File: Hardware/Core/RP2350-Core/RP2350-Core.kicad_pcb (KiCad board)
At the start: 2 copper layers, 62 parts, among them CN10 PR5L4015-5P-C-F, CN11 PR5L4015-5P-C-F, CN7 PR5L4015-5P-C-F, CN8 PR5L4015-5P-C-F, CN9 PR5L4015-5P-C-F, J7 SWD, J9 Conn_01x10_Socket, Q2 2N7002, Q3 2N7002, SW1 TS-1187A-B-A-B, SW2 TS-1187A-B-A-B, U19 W25Q16JVSNIQ, U2 AP2112K-3.3, U3 LM66200DRLR, U35 PR5L5015-5P-C-H, U36 PR5L5015-5P-C-H, U37 PR5L5015-5P-C-H, U38 PR5L5015-5P-C-H, U39 PR5L5015-5P-C-H, U4 RP2350A, Y1 Crystal

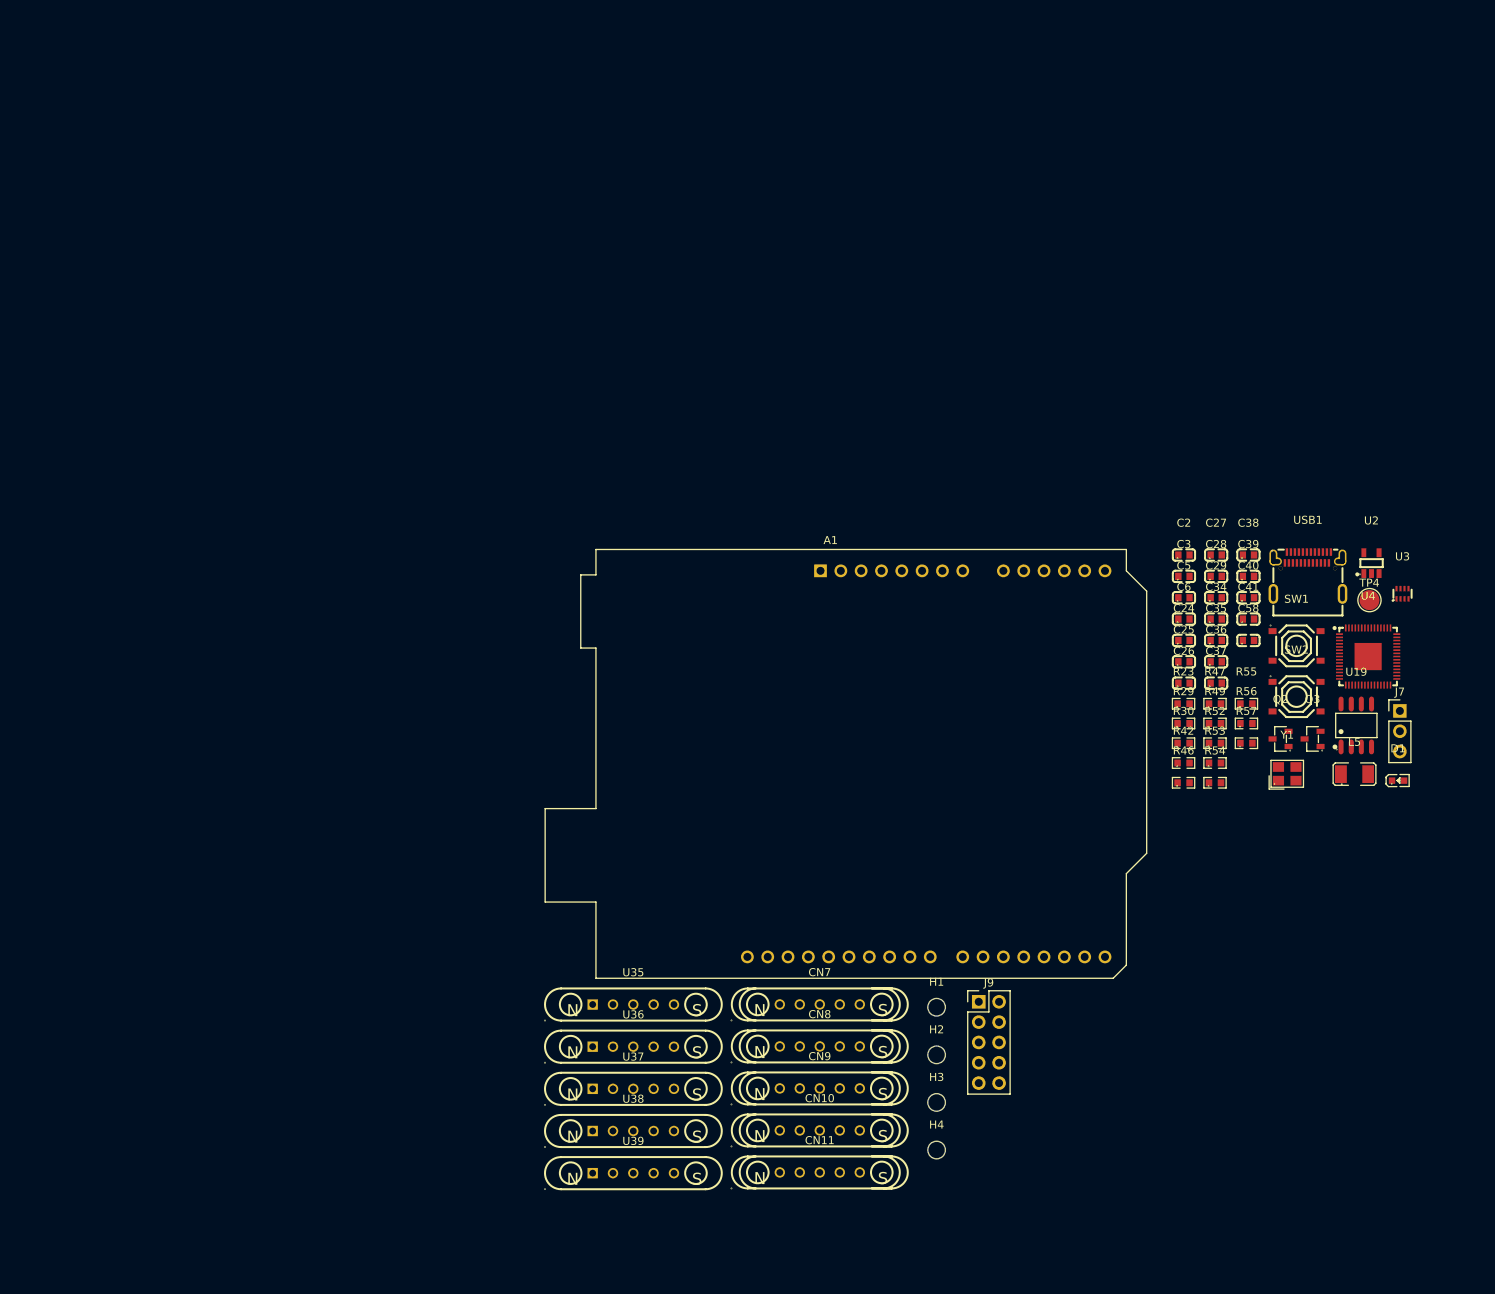
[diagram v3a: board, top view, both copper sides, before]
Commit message: Placed footprints RP235x
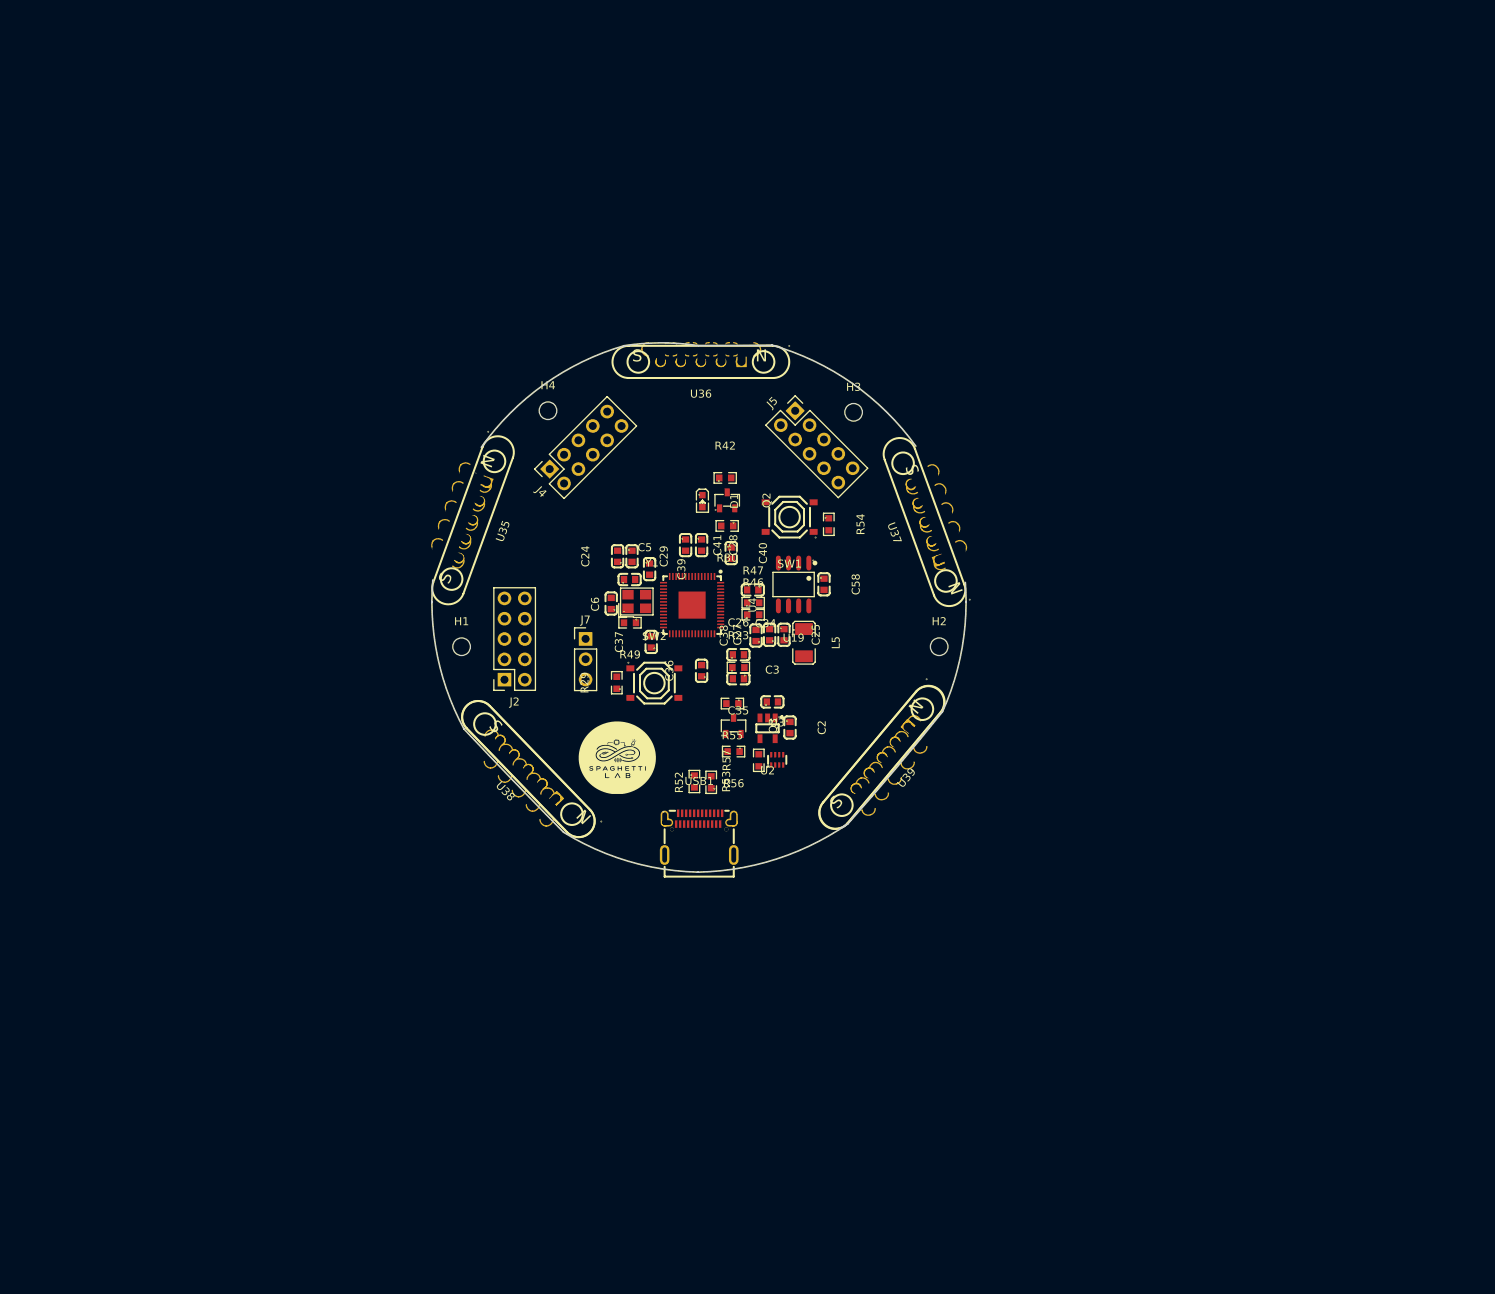
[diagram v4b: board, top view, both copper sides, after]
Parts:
- removed A1: Arduino_UNO_R3, Module:Arduino_UNO_R3
- removed J9: Conn_01x10_Socket, Connector_PinHeader_2.54mm:PinHeader_2x05_P2.54mm_Vertical
- removed TP4: ~, TestPoint:TestPoint_Pad_D2.5mm
- added ?: , Pad_e185, F.Cu at (66.4, 94.8)
- added ?: , Pad_e189, F.Cu at (59.4, 87.6)
- added ?: , Pad_e166, F.Cu at (54.8, 60.7)
- added ?: , Pad_e182, F.Cu at (109.5, 89.6)
- added ?: , Pad_e180, F.Cu at (112.6, 85.8)
- added ?: , Pad_e168, F.Cu at (56.5, 56.0)
- added ?: , Pad_e188, F.Cu at (61.2, 89.4)
- added ?: , Pad_e184, F.Cu at (106.2, 93.5)
- added ?: , Pad_e186, F.Cu at (64.7, 93.0)
- added ?: , Pad_e174, F.Cu at (113.3, 53.9)
- added ?: , Pad_e187, F.Cu at (62.9, 91.2)
- added ?: , Pad_e172, F.Cu at (115.1, 58.7)
- added ?: , Pad_e177, F.Cu at (85.7, 37.6)
- added ?: , Pad_e179, F.Cu at (80.6, 37.6)
- added ?: , Pad_e178, F.Cu at (83.1, 37.6)
- added ?: , Pad_e169, F.Cu at (57.4, 53.6)
- added ?: , Pad_e175, F.Cu at (90.7, 37.6)
- added ?: , Pad_e167, F.Cu at (55.7, 58.4)
- added ?: , Pad_e181, F.Cu at (111.1, 87.7)
- added ?: , Pad_e190, F.Cu at (54.0, 63.1)
- added ?: , Pad_e170, F.Cu at (116.8, 63.4)
- added ?: , Pad_e183, F.Cu at (107.8, 91.6)
- added ?: , Pad_e173, F.Cu at (114.2, 56.3)
- added ?: , Pad_e176, F.Cu at (88.2, 37.6)
- added ?: , Pad_e171, F.Cu at (115.9, 61.0)
- added J2: Conn_02x05_Counter_Clockwise, Connector_PinSocket_2.54mm:PinSocket_2x05_P2.54mm_Vertical, F.Cu at (61.1, 78.9)
- added J4: Conn_02x05_Counter_Clockwise, Connector_PinSocket_2.54mm:PinSocket_2x05_P2.54mm_Vertical, F.Cu at (66.7, 52.6)
- added J5: Conn_02x05_Counter_Clockwise, Connector_PinSocket_2.54mm:PinSocket_2x05_P2.54mm_Vertical, F.Cu at (97.4, 45.3)
- added U38: , USBC_PD_mo-easyedapro:CONN-TH_PR5L5015-5P-C-H, F.Cu at (64.1, 90.1)
- added U39: , USBC_PD_mo-easyedapro:CONN-TH_PR5L5015-5P-C-H, F.Cu at (108.2, 88.7)
- CN10, CN11, CN7, CN8, CN9: moved to B.Cu
- moved H4 104.4 mm to (66.5, 45.3)
- moved J7 102.2 mm to (71.2, 73.8)
- moved D1 93.7 mm to (85.8, 56.6), turned to -90 degrees
- moved CN9 92.0 mm to (85.6, 39.2), turned to 180 degrees
- moved H3 86.9 mm to (104.7, 45.5)
- moved U36 86.0 mm to (85.6, 39.2), turned to 180 degrees
- moved U4 84.7 mm to (84.5, 69.6), turned to -90 degrees
- moved Y1 84.1 mm to (77.6, 69.2)
- moved USB1 82.8 mm to (85.4, 98.2)
- moved U3 80.9 mm to (95.2, 88.9)
- moved SW2 80.3 mm to (79.8, 79.3)
- moved U37 79.6 mm to (113.6, 59.2), turned to 110 degrees
- moved CN8 78.8 mm to (57.1, 59.0), turned to -110 degrees
- moved U2 78.3 mm to (94.0, 85.0), turned to 180 degrees
- moved CN10 77.1 mm to (113.6, 59.3), turned to 110 degrees
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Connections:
- net /InOut (page 4)/~{RESET} renamed /Logic/~{RESET}
- SW1 pad 2: /Logic/QSPI_SS -> /InOut (page 4)/QSPI_SS
- U19 pad 1: /Logic/QSPI_SS -> /InOut (page 4)/QSPI_SS
- U19 pad 2: /Logic/QSPI_SD1 -> /InOut (page 4)/QSPI_SD1
- U19 pad 3: /Logic/QSPI_SD2 -> /InOut (page 4)/QSPI_SD2
- U19 pad 5: /Logic/QSPI_SD0 -> /InOut (page 4)/QSPI_SD0
- U19 pad 6: /Logic/QSPI_SCLK -> /InOut (page 4)/QSPI_SCLK
- U19 pad 7: /Logic/QSPI_SD3 -> /InOut (page 4)/QSPI_SD3
- U4 pad 55: /Logic/QSPI_SD3 -> /InOut (page 4)/QSPI_SD3
- U4 pad 56: /Logic/QSPI_SCLK -> /InOut (page 4)/QSPI_SCLK
- U4 pad 57: /Logic/QSPI_SD0 -> /InOut (page 4)/QSPI_SD0
- U4 pad 58: /Logic/QSPI_SD2 -> /InOut (page 4)/QSPI_SD2
- U4 pad 59: /Logic/QSPI_SD1 -> /InOut (page 4)/QSPI_SD1
- U4 pad 60: /Logic/QSPI_SS -> /InOut (page 4)/QSPI_SS
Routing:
- added copper zone on B.Cu, net VEXT
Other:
- board outline added: 66.8 x 66.2 mm
